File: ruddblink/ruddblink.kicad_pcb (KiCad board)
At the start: 2 copper layers, 38.1 x 45.7 mm, 33 parts, among them Q1 IRFML8244, SW1 JS202011JCQN, SW2 PTS526 SK15 SMTR2 LFS, U1 ATtiny85-20SU, U2 74HC595

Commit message: Begin routing
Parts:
- H1: footprint MountingHole:MountingHole_4.3mm_M4_Pad_Via -> ruddblink:MountingHole_Keyring
- moved R2 0.25 mm to (219.2, 52.6)
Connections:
- SW1 pad 1: Net-(F1-Pad2) -> VDD
- SW1 pad 2: VDD -> Net-(F1-Pad2)
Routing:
- net VDD: track 5.13 -> 47.0 mm
- net Net-(D5-Pad2): track 0.00 -> 40.2 mm, vias 0 -> 1
- net /SER: track 0.00 -> 33.1 mm
- net Net-(D4-Pad2): track 0.00 -> 31.3 mm, vias 0 -> 1
- net Net-(D3-Pad2): track 0.00 -> 22.0 mm, vias 0 -> 1
- net Net-(D7-Pad2): track 0.00 -> 21.2 mm, vias 0 -> 1
- net Net-(D2-Pad2): track 0.00 -> 13.6 mm, vias 0 -> 1
- net /LED8: track 15.3 -> 24.1 mm
- net Net-(D8-Pad2): track 0.00 -> 8.06 mm, vias 0 -> 1
- net /LED4: track 0.83 -> 8.22 mm
- net /LED7: track 13.6 -> 20.8 mm
- net /LED6: track 0.00 -> 6.85 mm
- net /BAT+: track 0.00 -> 5.84 mm
- net Net-(F1-Pad2): track 0.00 -> 4.75 mm
- net /USER: track 9.03 -> 13.8 mm
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- added copper zone on F.Cu, net (none)
- added copper zone on B.Cu, net GND
- added copper zone on F.Cu, net GND
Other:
- net class PowerThick added: clearance 0.381, trace_width 1.27, via_dia 1.016, via_drill 0.508
- board text added: "JLCJLCJLCJLC"
- board text removed: "RuddBlink"
- board text removed: "Virtutis mammilas exsugimus"
- board text removed: "v0.1"

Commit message: Rename pushbutton footprint
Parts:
- SW2: footprint ruddock-crest-blinky:SW_SPST_PTS526 -> ruddblink:SW_Push_PTS526
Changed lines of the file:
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@@
     (add_net "Net-(F1-Pad2)")
+  )
+  (module ruddblink:SW_Push_PTS526 (layer B.Cu)
+    (at 196.85 64.77 90)
+    (descr "C&K Components SPST SMD PTS645 Series 6mm Tact Switch")
+    (tags "SPST Button Switch")
+    (attr smd)
+    (fp_text reference SW2 (at 0 3.81 90) (layer B.SilkS)
+      (effects (font (size 1 1) (thickness 0.15)) (justify mirror))
+    )
+    (fp_text value "PTS526 SK15 SMTR2 LFS " (at 0 -4.15 90) (layer B.Fab)
+      (effects (font (size 1 1) (thickness 0.15)) (justify mirror))
+    )
+    (fp_circle (center 0 0) (end 1.75 0.05) (layer B.Fab) (width 0.1))
+    (fp_line (start -1.143 -2.794) (end 1.143 -2.794) (layer B.SilkS) (width 0.12))
+    (fp_line (start -2.794 1.143) (end -2.794 -1.143) (layer B.SilkS) (width 0.12))
+    (fp_line (start -1.143 2.794) (end 1.143 2.794) (layer B.SilkS) (width 0.12))
+    (fp_line (start 2.794 1.143) (end 2.794 -1.143) (layer B.SilkS) (width 0.12))
+    (fp_line (start -4.064 3.048) (end 4.064 3.048) (layer B.CrtYd) (width 0.05))
+    (fp_line (start -4.064 -3.048) (end 4.064 -3.048) (layer B.CrtYd) (width 0.05))
+    (fp_line (start -4.064 3.048) (end -4.064 -3.048) (layer B.CrtYd) (width 0.05))
+    (fp_line (start 4.064 -3.048) (end 4.064 3.048) (layer B.CrtYd) (width 0.05))
+    (fp_line (start 3 3) (end -3 3) (layer B.Fab) (width 0.1))
+    (fp_line (start 3 -3) (end 3 3) (layer B.Fab) (width 0.1))
+    (fp_line (start -3 -3) (end 3 -3) (layer B.Fab) (width 0.1))
+    (fp_line (start -3 3) (end -3 -3) (layer B.Fab) (width 0.1))
+    (fp_text user %R (at 0 3.81 90) (layer B.Fab)
+      (effects (font (size 1 1) (thickness 0.15)) (justify mirror))
+    )
+    (pad 2 smd rect (at 3.2 -1.85 90) (size 1.5 0.8) (layers B.Cu B.Paste B.Mask)
+      (net 1 GND))
+    (pad 1 smd rect (at 3.2 1.85 90) (size 1.5 0.8) (layers B.Cu B.Paste B.Mask)
+      (net 15 /USER))
+    (pad 1 smd rect (at -3.2 1.85 90) (size 1.5 0.8) (layers B.Cu B.Paste B.Mask)
+      (net 15 /USER))
+    (pad 2 smd rect (at -3.2 -1.85 90) (size 1.5 0.8) (layers B.Cu B.Paste B.Mask)
+      (net 1 GND))
+    (model ${KISYS3DMOD}/Button_Switch_SMD.3dshapes/SW_SPST_PTS645.wrl
+      (at (xyz 0 0 0))
+      (scale (xyz 1 1 1))
+      (rotate (xyz 0 0 0))
+    )
   )
   (module crest:circle_cu_1in5 (layer F.Cu)
@@
     )
   )
-  (module ruddock-crest-blinky:SW_SPST_PTS526 (layer B.Cu)
-    (at 196.85 64.77 90)
-    (descr "C&K Components SPST SMD PTS645 Series 6mm Tact Switch")
-    (tags "SPST Button Switch")
-    (attr smd)
-    (fp_text reference SW2 (at 0 3.81 90) (layer B.SilkS)
-      (effects (font (size 1 1) (thickness 0.15)) (justify mirror))
-    )
-    (fp_text value "PTS526 SK15 SMTR2 LFS " (at 0 -4.15 90) (layer B.Fab)
-      (effects (font (size 1 1) (thickness 0.15)) (justify mirror))
-    )
-    (fp_circle (center 0 0) (end 1.75 0.05) (layer B.Fab) (width 0.1))
-    (fp_line (start -1.143 -2.794) (end 1.143 -2.794) (layer B.SilkS) (width 0.12))
-    (fp_line (start -2.794 1.143) (end -2.794 -1.143) (layer B.SilkS) (width 0.12))
-    (fp_line (start -1.143 2.794) (end 1.143 2.794) (layer B.SilkS) (width 0.12))
-    (fp_line (start 2.794 1.143) (end 2.794 -1.143) (layer B.SilkS) (width 0.12))
-    (fp_line (start -4.064 3.048) (end 4.064 3.048) (layer B.CrtYd) (width 0.05))
-    (fp_line (start -4.064 -3.048) (end 4.064 -3.048) (layer B.CrtYd) (width 0.05))
-    (fp_line (start -4.064 3.048) (end -4.064 -3.048) (layer B.CrtYd) (width 0.05))
-    (fp_line (start 4.064 -3.048) (end 4.064 3.048) (layer B.CrtYd) (width 0.05))
-    (fp_line (start 3 3) (end -3 3) (layer B.Fab) (width 0.1))
-    (fp_line (start 3 -3) (end 3 3) (layer B.Fab) (width 0.1))
-    (fp_line (start -3 -3) (end 3 -3) (layer B.Fab) (width 0.1))
-    (fp_line (start -3 3) (end -3 -3) (layer B.Fab) (width 0.1))
-    (fp_text user %R (at 0 3.81 90) (layer B.Fab)
-      (effects (font (size 1 1) (thickness 0.15)) (justify mirror))
-    )
-    (pad 2 smd rect (at 3.2 -1.85 90) (size 1.5 0.8) (layers B.Cu B.Paste B.Mask)
-      (net 1 GND))
-    (pad 1 smd rect (at 3.2 1.85 90) (size 1.5 0.8) (layers B.Cu B.Paste B.Mask)
-      (net 15 /USER))
-    (pad 1 smd rect (at -3.2 1.85 90) (size 1.5 0.8) (layers B.Cu B.Paste B.Mask)
-      (net 15 /USER))
-    (pad 2 smd rect (at -3.2 -1.85 90) (size 1.5 0.8) (layers B.Cu B.Paste B.Mask)
-      (net 1 GND))
-    (model ${KISYS3DMOD}/Button_Switch_SMD.3dshapes/SW_SPST_PTS645.wrl
-      (at (xyz 0 0 0))
-      (scale (xyz 1 1 1))
-      (rotate (xyz 0 0 0))
-    )
-  )
   (module ruddock-crest-blinky:BatteryHolder_Keystone_3034_Wide (layer B.Cu)
     (at 212.09 78.232 180)
@@
     (min_thickness 0.254)
     (keepout (tracks allowed) (vias allowed) (copperpour not_allowed))
-    (fill (arc_segments 32) (thermal_gap 0.508) (thermal_bridge_width 0.508) (smoothing fillet) (radius 19.685))
+    (fill (arc_segments 32) (thermal_gap 0.508) (thermal_bridge_width 0.508))
     (polygon
       (pts

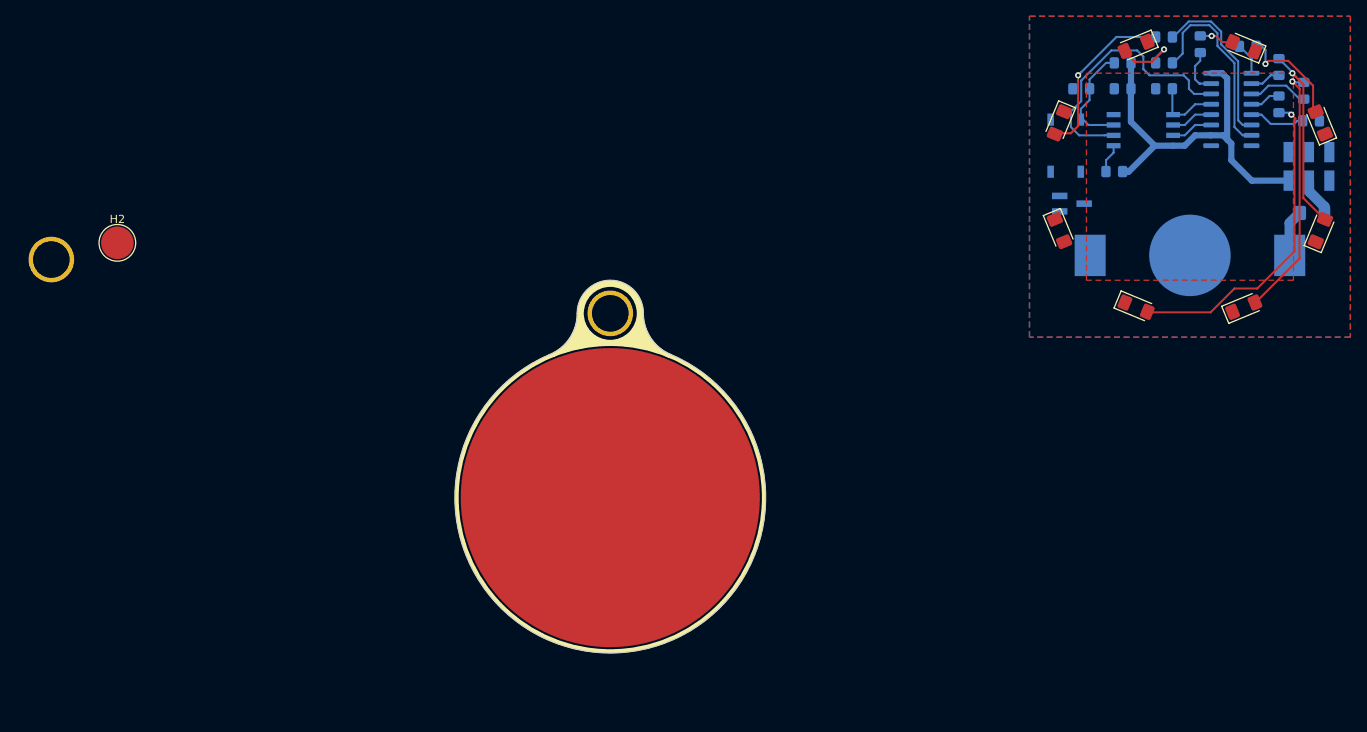
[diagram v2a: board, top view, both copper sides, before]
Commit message: Did most routing
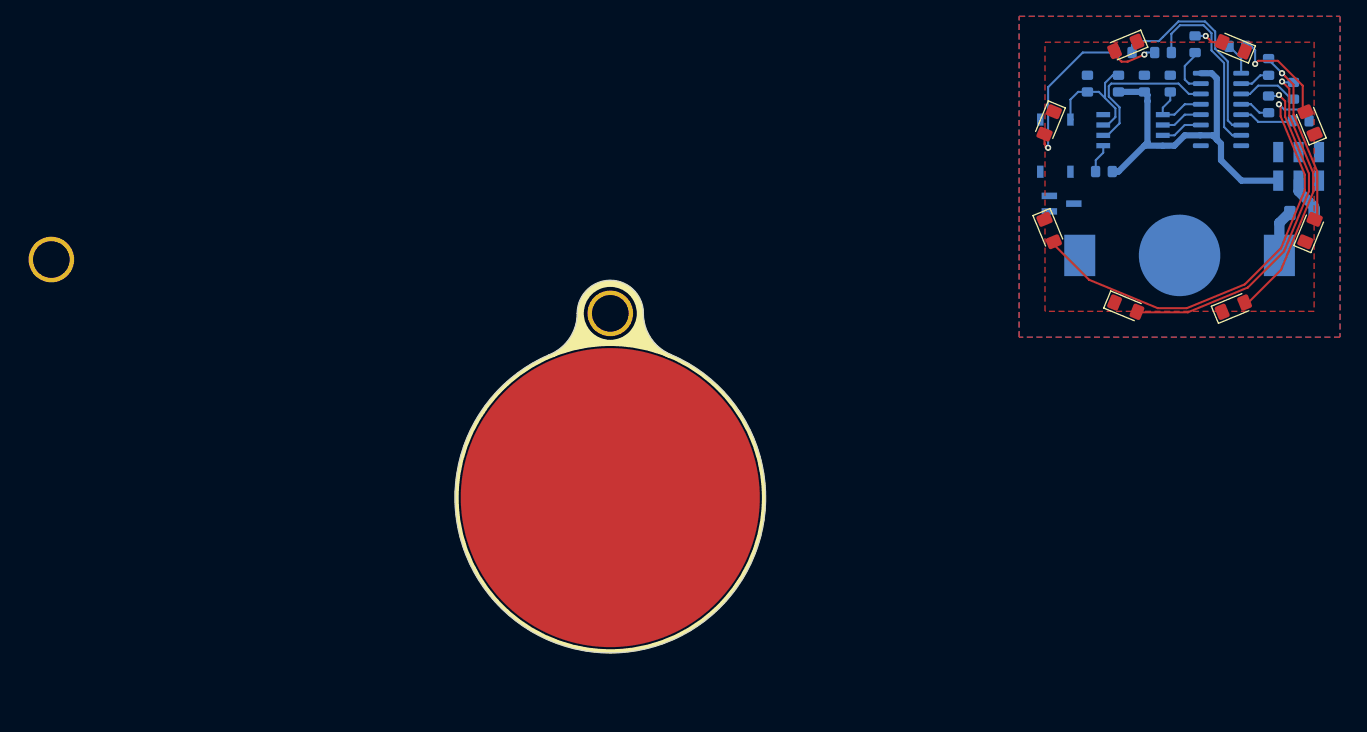
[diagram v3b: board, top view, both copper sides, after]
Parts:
- removed H2: CREST, TestPoint:TestPoint_Pad_D4.0mm
- moved R7 5.31 mm to (204.0, 53.3)
- moved C1 2.74 mm to (206.5, 57.1), turned to 90 degrees
- moved R11 2.59 mm to (203.3, 57.1), turned to 90 degrees
- moved R8 1.28 mm to (208.8, 53.3)
- moved R3 1.27 mm to (221.7, 55.1)
- moved BT1 1.27 mm to (210.8, 78.2)
- moved D2 1.27 mm to (226.8, 62.0)
- moved D3 1.27 mm to (226.8, 75.2)
- moved F1 1.27 mm to (225.8, 73.0)
- moved R2 1.27 mm to (217.9, 52.6)
- moved R4 1.27 mm to (224.8, 58.0)
- moved R5 1.27 mm to (221.7, 59.7), turned to 90 degrees
- moved R6 1.27 mm to (225.7, 61.7)
- moved R9 1.27 mm to (201.5, 67.9)
- moved U1 1.27 mm to (205.1, 62.9)
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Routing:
- net Net-(D6-Pad2): track 0.00 -> 56.9 mm, vias 0 -> 1
- net /SER: track 33.1 -> 19.7 mm
- net /LED7: track 20.8 -> 26.2 mm
- net Net-(D5-Pad2): track 40.2 -> 43.0 mm
- net /USER: track 13.8 -> 16.3 mm
- net Net-(D7-Pad2): track 21.2 -> 19.3 mm
- net Net-(D8-Pad2): track 8.06 -> 6.47 mm
- net /LED8: track 24.1 -> 22.7 mm
- net VDD: track 47.0 -> 45.8 mm
- net Net-(D4-Pad2): track 31.3 -> 32.3 mm
- net Net-(D1-Pad2): track 4.26 -> 3.62 mm
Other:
- net class Power: clearance 0.381 -> 0.254
- net class PowerThick: clearance 0.381 -> 0.254
- rule trace_min: 0.2 -> 0.2032

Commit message: Finish routing
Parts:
- removed G***: LOGO, crest:circle_cu_1in5
- removed G***: LOGO, crest:ruddock_mask_1in5
- removed REF**: MountingHole_3.2mm_M3_DIN965_Pad, MountingHole:MountingHole_3.2mm_M3_DIN965_Pad
- SW1: footprint ruddock-crest-blinky:SW_SPDT_CK-JS202011JCQN -> ruddblink:SW_SPDT_CK-JS202011JCQN
- moved H1 68.9 mm to (141.0, 85.3)
- moved R7 0.52 mm to (204.1, 52.8)
- moved R8 0.51 mm to (208.8, 52.8)
- moved SW2 0.25 mm to (195.8, 64.8)
- moved Q1 0.13 mm to (196.3, 72.0)
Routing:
- net /BAT-: track 0.00 -> 15.6 mm
- net VDD: track 45.8 -> 57.4 mm
- net GND: track 0.00 -> 2.70 mm, vias 0 -> 2
- net Net-(D8-Pad2): track 6.47 -> 8.82 mm
- net Net-(D4-Pad2): track 32.3 -> 33.1 mm
- net Net-(D7-Pad2): track 19.3 -> 20.0 mm
- net Net-(D5-Pad2): track 43.0 -> 43.5 mm

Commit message: Position designators
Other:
- board text added: "+"
- board text added: "CENT NEG"
- board text added: "NC"
- board text added: "RuddBlink"
- board text added: "v0.1"
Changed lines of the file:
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@@
   (general
     (thickness 1.6)
-    (drawings 50)
+    (drawings 55)
     (tracks 212)
     (zones 0)
@@
     (39 F.Mask user)
     (40 Dwgs.User user)
-    (41 Cmts.User user)
-    (42 Eco1.User user)
-    (43 Eco2.User user)
+    (41 Cmts.User user hide)
+    (42 Eco1.User user hide)
+    (43 Eco2.User user hide)
     (44 Edge.Cuts user)
-    (45 Margin user)
+    (45 Margin user hide)
     (46 B.CrtYd user)
     (47 F.CrtYd user)
@@
     (tags "switch spdt")
     (attr smd)
-    (fp_text reference SW1 (at 0 4.064) (layer B.SilkS)
+    (fp_text reference SW1 (at -5.588 0 90) (layer B.SilkS)
       (effects (font (size 1 1) (thickness 0.15)) (justify mirror))
     )
@@
     (tags "SPST Button Switch")
     (attr smd)
-    (fp_text reference SW2 (at 0 3.81 90) (layer B.SilkS)
+    (fp_text reference SW2 (at 0 3.683 90) (layer B.SilkS)
       (effects (font (size 1 1) (thickness 0.15)) (justify mirror))
     )
@@
     (tags "Keystone type 3034 coin cell retainer")
     (attr smd)
-    (fp_text reference BT1 (at 15.494 1.27 90) (layer B.SilkS)
+    (fp_text reference BT1 (at -11.684 4.318 90) (layer B.SilkS)
       (effects (font (size 1 1) (thickness 0.15)) (justify mirror))
     )
@@
     (tags "SOIC 1.27")
     (attr smd)
-    (fp_text reference U1 (at 0 3.68) (layer B.SilkS)
+    (fp_text reference U1 (at -5.588 -1.905 90) (layer B.SilkS)
       (effects (font (size 1 1) (thickness 0.15)) (justify mirror))
     )
@@
     (tags SOT-23)
     (attr smd)
-    (fp_text reference Q1 (at 0 2.5) (layer B.SilkS)
+    (fp_text reference Q1 (at 1.905 -1.524) (layer B.SilkS)
       (effects (font (size 1 1) (thickness 0.15)) (justify mirror))
     )
@@
     (tags "resistor handsolder")
     (attr smd)
-    (fp_text reference F1 (at 0 1.82) (layer B.SilkS)
+    (fp_text reference F1 (at -3.5925 -1.651) (layer B.SilkS)
       (effects (font (size 1 1) (thickness 0.15)) (justify mirror))
     )
@@
     (tags "resistor handsolder")
     (attr smd)
-    (fp_text reference R5 (at 0 1.65 90) (layer B.SilkS)
+    (fp_text reference R5 (at -2.912 0.127 90) (layer B.SilkS)
       (effects (font (size 1 1) (thickness 0.15)) (justify mirror))
     )
@@
     (tags "resistor handsolder")
     (attr smd)
-    (fp_text reference R4 (at 0 1.65 90) (layer B.SilkS)
+    (fp_text reference R4 (at -1.025 1.778 90) (layer B.SilkS)
       (effects (font (size 1 1) (thickness 0.15)) (justify mirror))
     )
@@
     (tags "resistor handsolder")
     (attr smd)
-    (fp_text reference R3 (at 0 1.65 90) (layer B.SilkS)
+    (fp_text reference R3 (at -1.025 -1.524 90) (layer B.SilkS)
       (effects (font (size 1 1) (thickness 0.15)) (justify mirror))
     )
@@
     (tags "resistor handsolder")
     (attr smd)
-    (fp_text reference R2 (at 0 1.65) (layer B.SilkS)
+    (fp_text reference R2 (at 0.771 1.651) (layer B.SilkS)
       (effects (font (size 1 1) (thickness 0.15)) (justify mirror))
     )
@@
     (tags "resistor handsolder")
     (attr smd)
-    (fp_text reference R9 (at 0 1.65) (layer B.SilkS)
+    (fp_text reference R9 (at 0.88 -1.778) (layer B.SilkS)
       (effects (font (size 1 1) (thickness 0.15)) (justify mirror))
     )
@@
     )
   )
+  (gr_text NC (at 194.818 76.454) (layer B.SilkS)
+    (effects (font (size 1.27 1.27) (thickness 0.254)) (justify mirror))
+  )
+  (gr_text v0.1 (at 205.486 67.31) (layer B.SilkS)
+    (effects (font (size 1.016 1.016) (thickness 0.1524)) (justify mirror))
+  )
+  (gr_text RuddBlink (at 213.106 67.056) (layer B.SilkS)
+    (effects (font (size 1.524 1.524) (thickness 0.254)) (justify mirror))
+  )
+  (gr_text "CENT NEG" (at 196.596 74.549) (layer B.SilkS)
+    (effects (font (size 0.8128 0.8128) (thickness 0.1016)) (justify mirror))
+  )
+  (gr_text + (at 226.695 76.2) (layer B.SilkS)
+    (effects (font (size 2.032 2.032) (thickness 0.508)) (justify mirror))
+  )
   (gr_text JLCJLCJLCJLC (at 215.9 59.055 90) (layer B.SilkS)

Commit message: Finish board design
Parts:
- added G***: LOGO, crest:ruddock_mask_1in125, F.Cu at (142.2, 114.9)
- BT1: footprint ruddock-crest-blinky:BatteryHolder_Keystone_3034_Wide -> ruddblink:BatteryHolder_Keystone_3034_Wide
- moved C1 82.4 mm to (137.9, 102.9)
- moved R7 82.4 mm to (135.5, 98.6)
- moved R8 82.4 mm to (140.2, 98.6)
- moved C3 82.4 mm to (130.9, 102.9)
- moved D1 82.4 mm to (148.8, 98.4)
- moved D2 82.4 mm to (158.2, 107.7)
- moved D3 82.4 mm to (158.2, 120.9)
- moved D4 82.4 mm to (148.8, 130.3)
- moved D5 82.4 mm to (135.6, 130.3)
- moved D6 82.4 mm to (126.2, 120.9)
- moved D7 82.4 mm to (126.2, 107.7)
- moved D8 82.4 mm to (135.6, 98.3)
- moved F1 82.4 mm to (157.3, 118.7)
- moved Q1 82.4 mm to (127.8, 117.7)
- moved R10 82.4 mm to (141.1, 102.9)
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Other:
- board size 38.1 x 45.7 mm -> 40.6 x 48.5 mm
- board text removed: "GRID: 50 MIL"
